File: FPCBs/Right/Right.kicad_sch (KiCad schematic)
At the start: 11 parts, among them J1 Conn_2Rows-35Pins, SW1 Mode Dial, SW2 ON/OFF

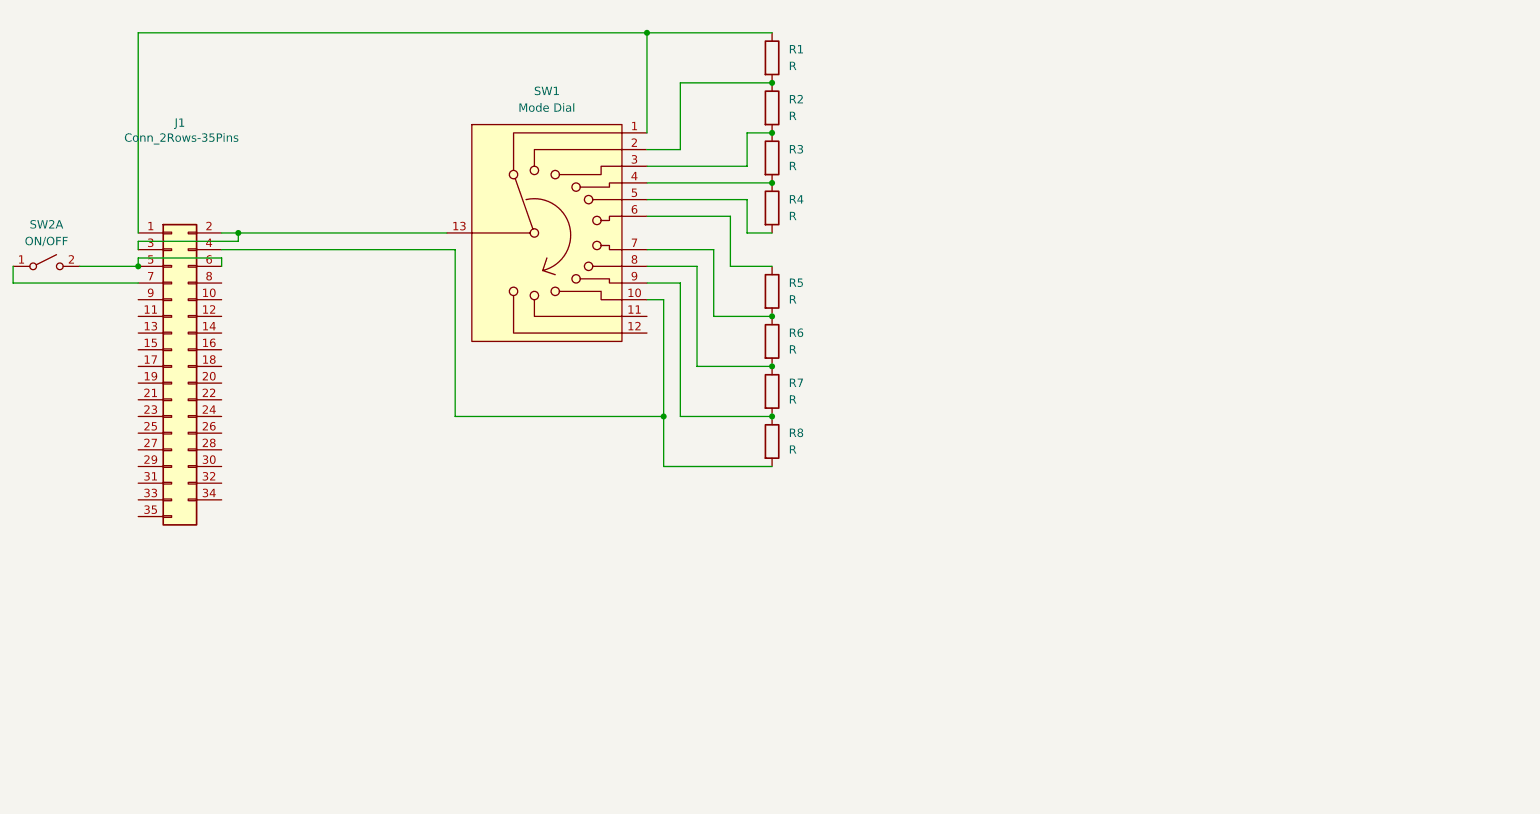
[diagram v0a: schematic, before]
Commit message: Finish schematic
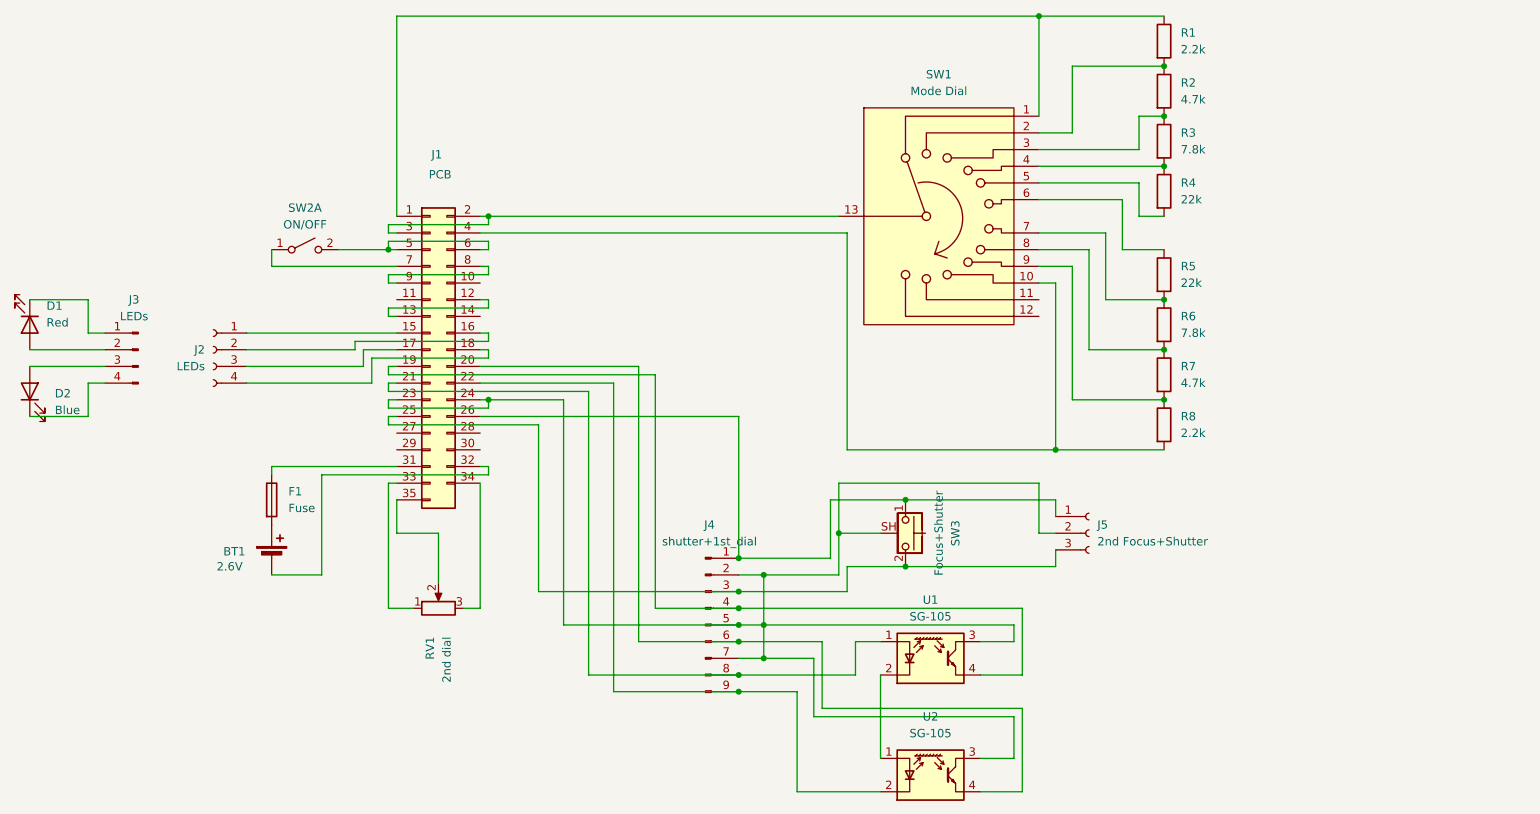
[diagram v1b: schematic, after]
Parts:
- added BT1: 2.6V, symbol Device:Battery_Cell
- added D1: Red, LED_SMD:LED_0402_1005Metric, symbol Device:LED
- added D2: Blue, LED_SMD:LED_0402_1005Metric, symbol Device:LED
- added F1: Fuse, Fuse:Fuse_0402_1005Metric, symbol Device:Fuse
- added J2: LEDs, symbol Connector:Conn_01x04_Socket
- added J3: LEDs, symbol Connector:Conn_01x04_Pin
- added J4: shutter+1st_dial, symbol Connector:Conn_01x09_Pin
- added J5: 2nd Focus+Shutter, symbol Connector:Conn_01x03_Socket
- added RV1: 2nd dial, symbol Device:R_Potentiometer
- added SW3: Focus+Shutter, Button_Switch_SMD:SW_SPST_CK_KMS2xxGP, symbol Switch:CK_KMS2xxGP
- added U1, U2: SG-105, OptoDevice:Kodenshi_SG105, symbol Sensor_Proximity:SG-105
- J1: value Conn_2Rows-35Pins -> PCB
- R1, R8: value R -> 2.2k; footprint (none) -> Resistor_SMD:R_0201_0603Metric
- R2, R7: value R -> 4.7k; footprint (none) -> Resistor_SMD:R_0201_0603Metric
- R3, R6: value R -> 7.8k; footprint (none) -> Resistor_SMD:R_0201_0603Metric
- R4, R5: value R -> 22k; footprint (none) -> Resistor_SMD:R_0201_0603Metric
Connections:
- net at J1.12 (Pin_12): now also J1.13 (Pin_13)
- net at J1.15 (Pin_15): now also J2.1 (Pin_1)
- net at J1.16 (Pin_16): now also J2.2 (Pin_2)
- net at J1.17 (Pin_17): now also J2.3 (Pin_3)
- net at J1.18 (Pin_18): now also J2.4 (Pin_4)
- net at J1.19 (Pin_19): now also J4.4 (Pin_4), U1.4 (E)
- net at J1.20 (Pin_20): now also J4.6 (Pin_6), U2.4 (E)
- net at J1.21 (Pin_21): now also J4.8 (Pin_8), U1.1 (A)
- net at J1.22 (Pin_22): now also J4.9 (Pin_9), U2.2 (K)
- net at J1.23 (Pin_23): now also J1.24 (Pin_24), J4.2 (Pin_2), J4.5 (Pin_5), J4.7 (Pin_7), J5.2 (Pin_2), SW3.SH (B), U1.3 (C), U2.3 (C)
- net at J1.25 (Pin_25): now also J4.3 (Pin_3), J5.3 (Pin_3), SW3.2
- net at J1.26 (Pin_26): now also J4.1 (Pin_1), J5.1 (Pin_1), SW3.1
- net at J1.31 (Pin_31): now also F1.1
- net at J1.32 (Pin_32): now also BT1.2 (-)
- net at J1.33 (Pin_33): now also RV1.1
- net at J1.34 (Pin_34): now also RV1.3
- net at J1.35 (Pin_35): now also RV1.2
- net at J1.8 (Pin_8): now also J1.9 (Pin_9)
- new net: U1.2 (K), U2.1 (A)
- new net: D2.1 (K), J3.4 (Pin_4)
- new net: D2.2 (A), J3.3 (Pin_3)
- new net: D1.1 (K), J3.1 (Pin_1)
- new net: D1.2 (A), J3.2 (Pin_2)
- new net: BT1.1 (+), F1.2
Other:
- moved on the sheet: J1, R1, R2, R3, R4, R5, R6, R7, R8, SW1, SW2A

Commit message: Add footprints
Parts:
- BT1: footprint (none) -> Leica-G9ii:Battery_Cell
- J1: footprint (none) -> Leica-G9ii:FPC-2Rows-35Pins-0.23mm
- J2, J3: footprint (none) -> Leica-G9ii:Connector-4Pins
- RV1: footprint (none) -> Leica-G9ii:2nd_dial
- SW1: footprint (none) -> Leica-G9ii:Switch_Modes
- SW3: footprint Button_Switch_SMD:SW_SPST_CK_KMS2xxGP -> Leica-G9ii:Switch_Shutter_1
- U1, U2: footprint OptoDevice:Kodenshi_SG105 -> Leica-G9ii:Opto_Switch
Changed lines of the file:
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@@
+	)
+	(junction
+		(at 157.48 110.49)
+		(diameter 0)
+		(color 0 0 0 0)
+	)
+	(junction
+		(at 157.48 100.33)
+		(diameter 0)
+		(color 0 0 0 0)
 	)
 	(junction
@@
 	)
 	(junction
-		(at 157.48 110.49)
-		(diameter 0)
-		(color 0 0 0 0)
-	)
-	(junction
 		(at 132.08 121.92)
 		(diameter 0)
@@
 		(color 0 0 0 0)
 	)
-	(junction
-		(at 157.48 100.33)
-		(diameter 0)
-		(color 0 0 0 0)
-	)
 	(wire
 		(pts
@@
 	(wire
 		(pts
+			(xy 157.48 110.49) (xy 180.34 110.49)
+		)
+		(stroke
+			(width 0)
+			(type default)
+		)
+	)
+	(wire
+		(pts
 			(xy 78.74 80.01) (xy 78.74 81.28)
 		)
@@
 	(wire
 		(pts
+			(xy 157.48 100.33) (xy 180.34 100.33)
+		)
+		(stroke
+			(width 0)
+			(type default)
+		)
+	)
+	(wire
+		(pts
 			(xy 177.8 26.67) (xy 177.8 41.91)
 		)
@@
 	(wire
 		(pts
-			(xy 180.34 110.49) (xy 157.48 110.49)
-		)
-		(stroke
-			(width 0)
-			(type default)
-		)
-	)
-	(wire
-		(pts
 			(xy 132.08 116.84) (xy 175.26 116.84)
 		)
@@
 		(pts
 			(xy 148.59 110.49) (xy 157.48 110.49)
-		)
-		(stroke
-			(width 0)
-			(type default)
-		)
-	)
-	(wire
-		(pts
-			(xy 157.48 100.33) (xy 180.34 100.33)
 		)
 		(stroke
@@
 			)
 		)
-		(property "Footprint" ""
+		(property "Footprint" "Leica-G9ii:FPC-2Rows-35Pins-0.23mm"
 			(at 85.09 77.47 0)
 			(effects
@@
 			)
 		)
-		(property "Footprint" "OptoDevice:Kodenshi_SG105"
+		(property "Footprint" "Leica-G9ii:Opto_Switch"
 			(at 161.29 129.54 0)
 			(effects
@@
 			)
 		)
-		(property "Footprint" ""
+		(property "Footprint" "Leica-G9ii:Switch_Modes"
 			(at 162.56 39.37 0)
 			(effects
@@
 			)
 		)
-		(property "Footprint" "OptoDevice:Kodenshi_SG105"
+		(property "Footprint" "Leica-G9ii:Opto_Switch"
 			(at 161.29 147.32 0)
 			(effects
@@
 			)
 		)
-		(property "Footprint" "Button_Switch_SMD:SW_SPST_CK_KMS2xxGP"
+		(property "Footprint" "Leica-G9ii:Switch_Shutter_1"
 			(at 162.56 105.41 0)
 			(effects
@@
 			)
 		)
-		(property "Footprint" ""
+		(property "Footprint" "Leica-G9ii:Battery_Cell"
 			(at 60.96 107.696 90)
 			(effects
@@
 			)
 		)
-		(property "Footprint" ""
+		(property "Footprint" "Leica-G9ii:Connector-4Pins"
 			(at 52.07 77.47 0)
 			(effects
@@
 			)
 		)
-		(property "Footprint" ""
+		(property "Footprint" "Leica-G9ii:2nd_dial"
 			(at 86.36 116.84 0)
 			(effects
@@
 			)
 		)
-		(property "Footprint" ""
+		(property "Footprint" "Leica-G9ii:Connector-4Pins"
 			(at 40.64 77.47 0)
 			(effects

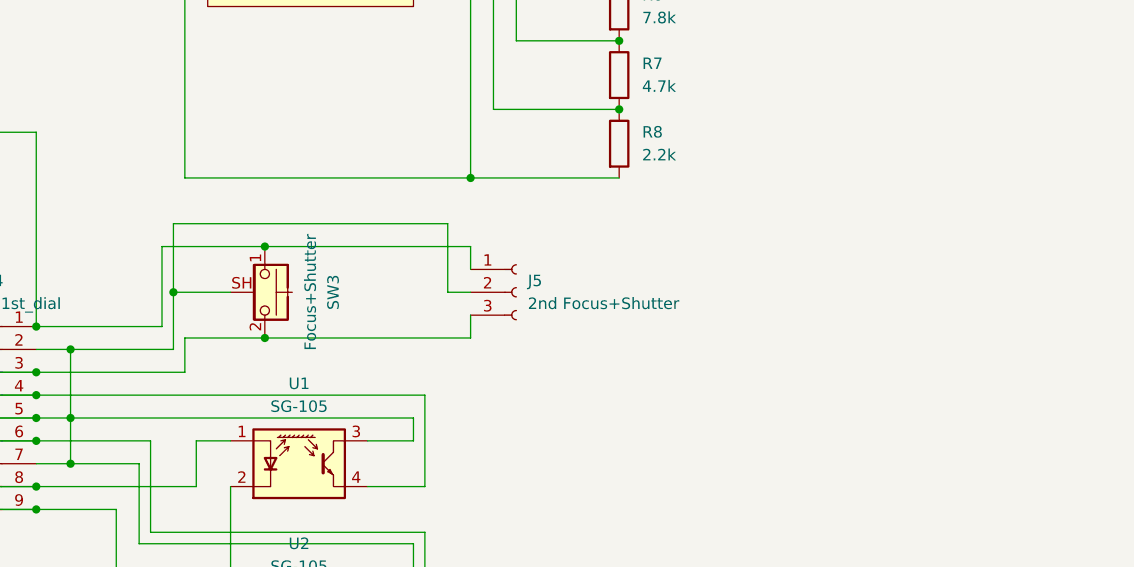
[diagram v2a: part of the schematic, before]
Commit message: Extend fpc size
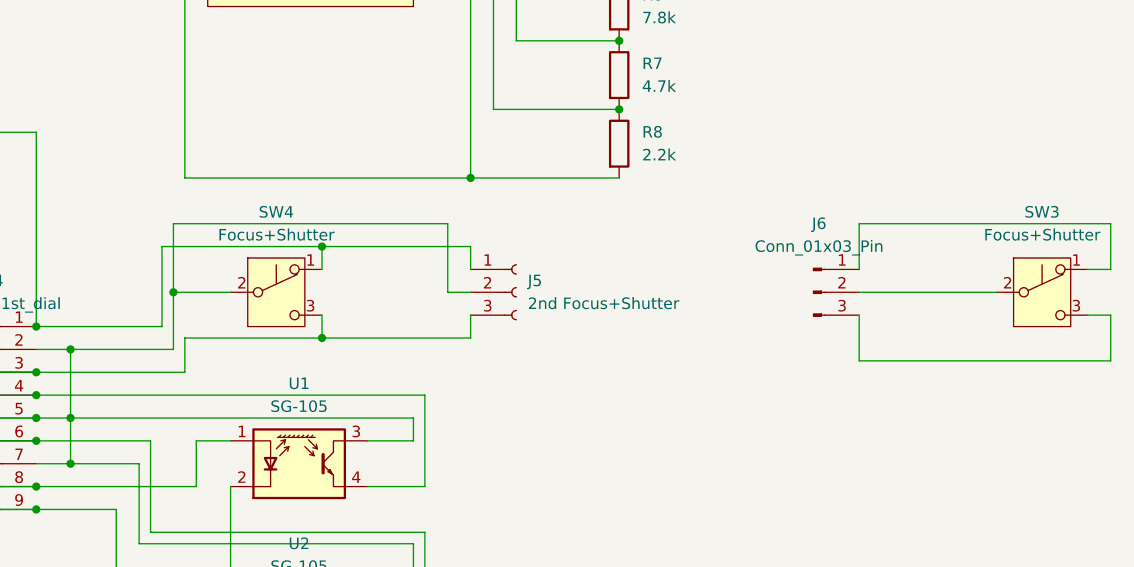
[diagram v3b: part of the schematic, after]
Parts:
- removed SW3: Focus+Shutter, Leica-G9ii:Switch_Shutter_1, symbol Switch:CK_KMS2xxGP
- added J6: Conn_01x03_Pin, Leica-G9ii:Connector-4Pins, symbol Connector:Conn_01x03_Pin
- added SW3, SW4: Focus+Shutter, Leica-G9ii:Switch_Shutter_1, symbol Switch:SW_Push_SPDT
- J5: footprint (none) -> Leica-G9ii:Connector-4Pins
- SW2: footprint (none) -> Leica-G9ii:Switch_Power
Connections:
- net at J1.23 (Pin_23), J1.24 (Pin_24), J4.2 (Pin_2)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: now also SW4.2 (B)
- net at J1.25 (Pin_25), J4.3 (Pin_3), J5.3 (Pin_3): now also SW4.3 (C)
- net at J1.26 (Pin_26), J4.1 (Pin_1), J5.1 (Pin_1): now also SW4.1 (A)
- new net: J6.1 (Pin_1), SW3.1 (A)
- new net: J6.2 (Pin_2), SW3.2 (B)
- new net: J6.3 (Pin_3), SW3.3 (C)

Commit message: Update the back pcb
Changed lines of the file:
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@@
 (kicad_sch
-	(version 20231120)
+	(version 20250114)
 	(generator "eeschema")
-	(generator_version "8.0")
+	(generator_version "9.0")
 	(paper "A4")
 	(junction
@@
 		)
 	)
+	(embedded_fonts no)
 )

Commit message: Update to kicad 9
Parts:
- J1: footprint Leica-G9ii:FPC-2Rows-35Pins-0.23mm -> Leica-G9ii:FPC-2Rows-35Pins-0.5mm
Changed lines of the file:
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@@
 			)
 		)
-		(property "Footprint" "Leica-G9ii:FPC-2Rows-35Pins-0.23mm"
+		(property "Footprint" "Leica-G9ii:FPC-2Rows-35Pins-0.5mm"
 			(at 85.09 77.47 0)
 			(effects
